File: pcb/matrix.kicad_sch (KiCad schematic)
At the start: 122 parts, among them SW1 SW_Push, SW10 SW_Push, SW11 SW_Push, SW12 SW_Push, SW13 SW_Push, SW14 SW_Push, SW15 SW_Push, SW16 SW_Push, SW17 SW_Push, SW18 SW_Push, SW19 SW_Push, SW2 SW_Push, SW20 SW_Push, SW21 SW_Push, SW22 SW_Push, SW23 SW_Push, SW24 SW_Push, SW25 SW_Push, SW26 SW_Push, SW27 SW_Push, SW28 SW_Push, SW29 SW_Push, SW3 SW_Push, SW30 SW_Push, SW31 SW_Push, SW32 SW_Push, SW33 SW_Push, SW34 SW_Push, SW35 SW_Push, SW36 SW_Push, SW37 SW_Push, SW38 SW_Push, SW39 SW_Push, SW4 SW_Push, SW40 SW_Push, SW41 SW_Push, SW42 SW_Push, SW43 SW_Push, SW44 SW_Push, SW45 SW_Push, SW46 SW_Push, SW47 SW_Push, SW48 SW_Push, SW49 SW_Push, SW5 SW_Push, SW50 SW_Push, SW51 SW_Push, SW52 SW_Push, SW53 SW_Push, SW54 SW_Push, SW55 SW_Push, SW56 SW_Push, SW57 SW_Push, SW58 SW_Push, SW59 SW_Push, SW6 SW_Push, SW60 SW_Push, SW61 SW_Push, SW7 SW_Push, SW8 SW_Push, SW9 SW_Push

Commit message: Fixed critical mistake where CAPSLOCK and Tab were indistinguishable
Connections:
- net COL0: no longer SW54.1
- net COL1: now also SW54.1; no longer SW55.1
- net COL2: now also SW55.1; no longer SW56.1
- net COL3: now also SW56.1; no longer SW57.1
- net COL4: now also SW57.1
- net ROW2: no longer D15.2 (A)
- net ROW4: now also D15.2 (A)
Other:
- note added: "TAB Moved to ROW4"
- note removed: "TAB is ROW2"
- moved on the sheet: D1, D15, D29, D42, D54, D55, D56, D57, SW1, SW15, SW29, SW42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

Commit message: Changed schematic header
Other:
- company: (none) -> agrantushinsky/simplekeyboard
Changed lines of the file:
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@@
 	(title_block
 		(title "Keyboard Matrix")
-		(date "2026-05-05")
+		(date "2026-07-18")
 		(rev "A")
+		(company "agrantushinsky/simplekeyboard")
 	)
 	(text "TAB Moved to ROW4"

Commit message: Changed spacebar to use reversed stabilizers
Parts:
- SW57: footprint ai03_MX:MX-Solderable-6.25U -> ai03_MX:MX-Solderable-6.25U-ReversedStabilizers
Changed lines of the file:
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@@
 			)
 		)
-		(property "Footprint" "ai03_MX:MX-Solderable-6.25U"
+		(property "Footprint" "ai03_MX:MX-Solderable-6.25U-ReversedStabilizers"
 			(at 115.57 121.92 0)
 			(effects

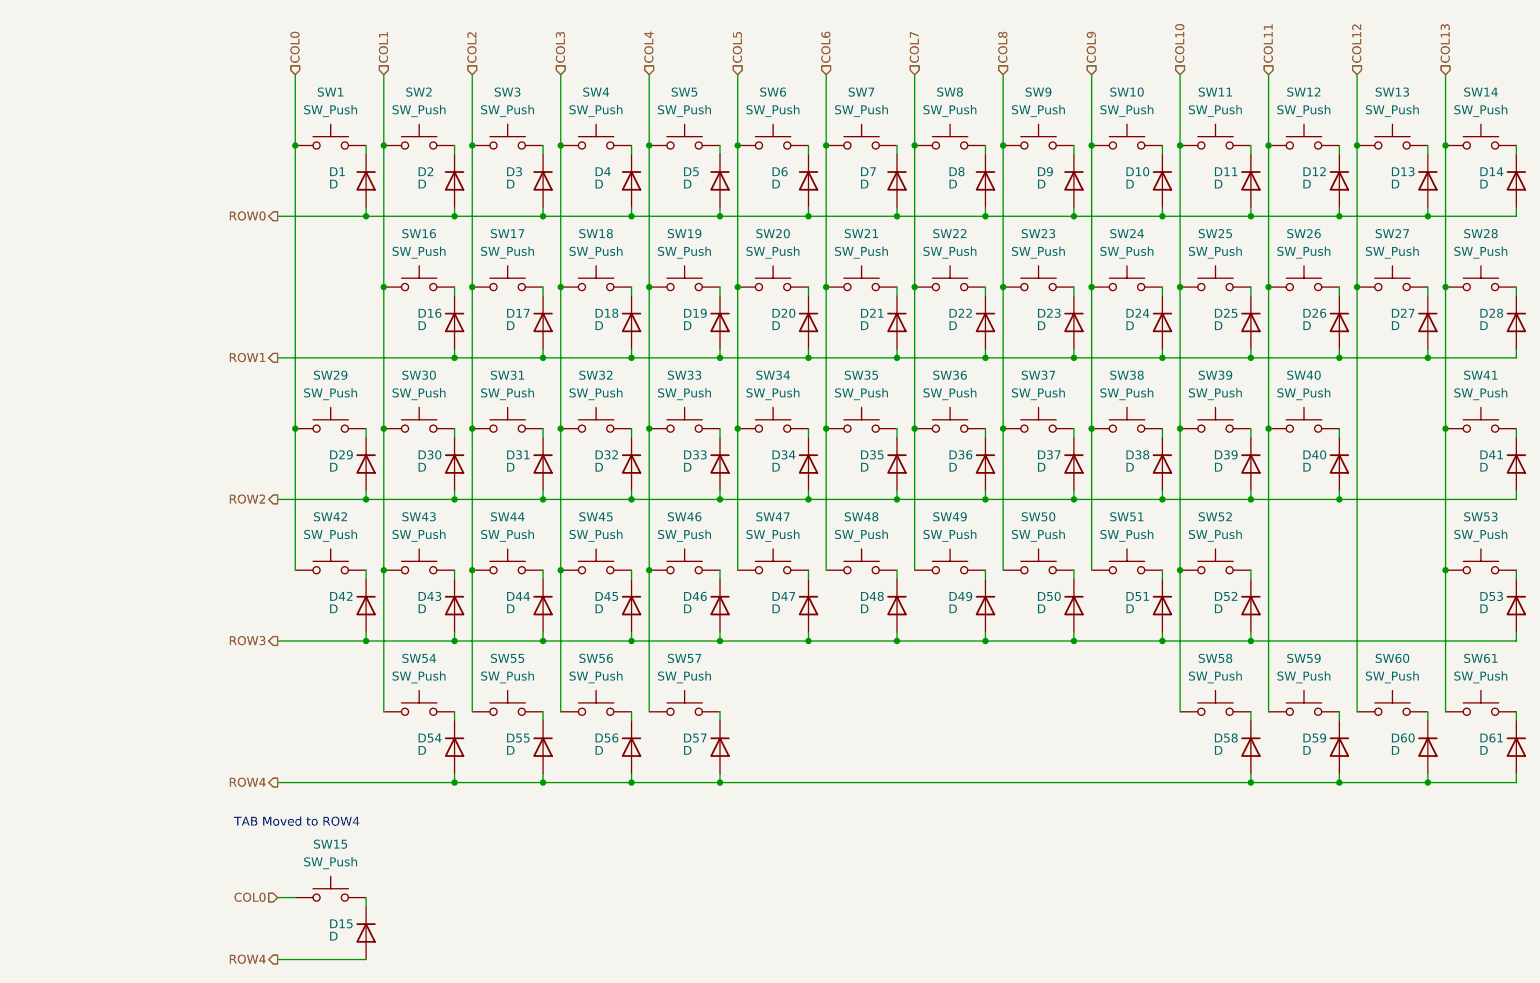
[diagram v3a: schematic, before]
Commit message: Fixed diode orientation and SDA/SCL
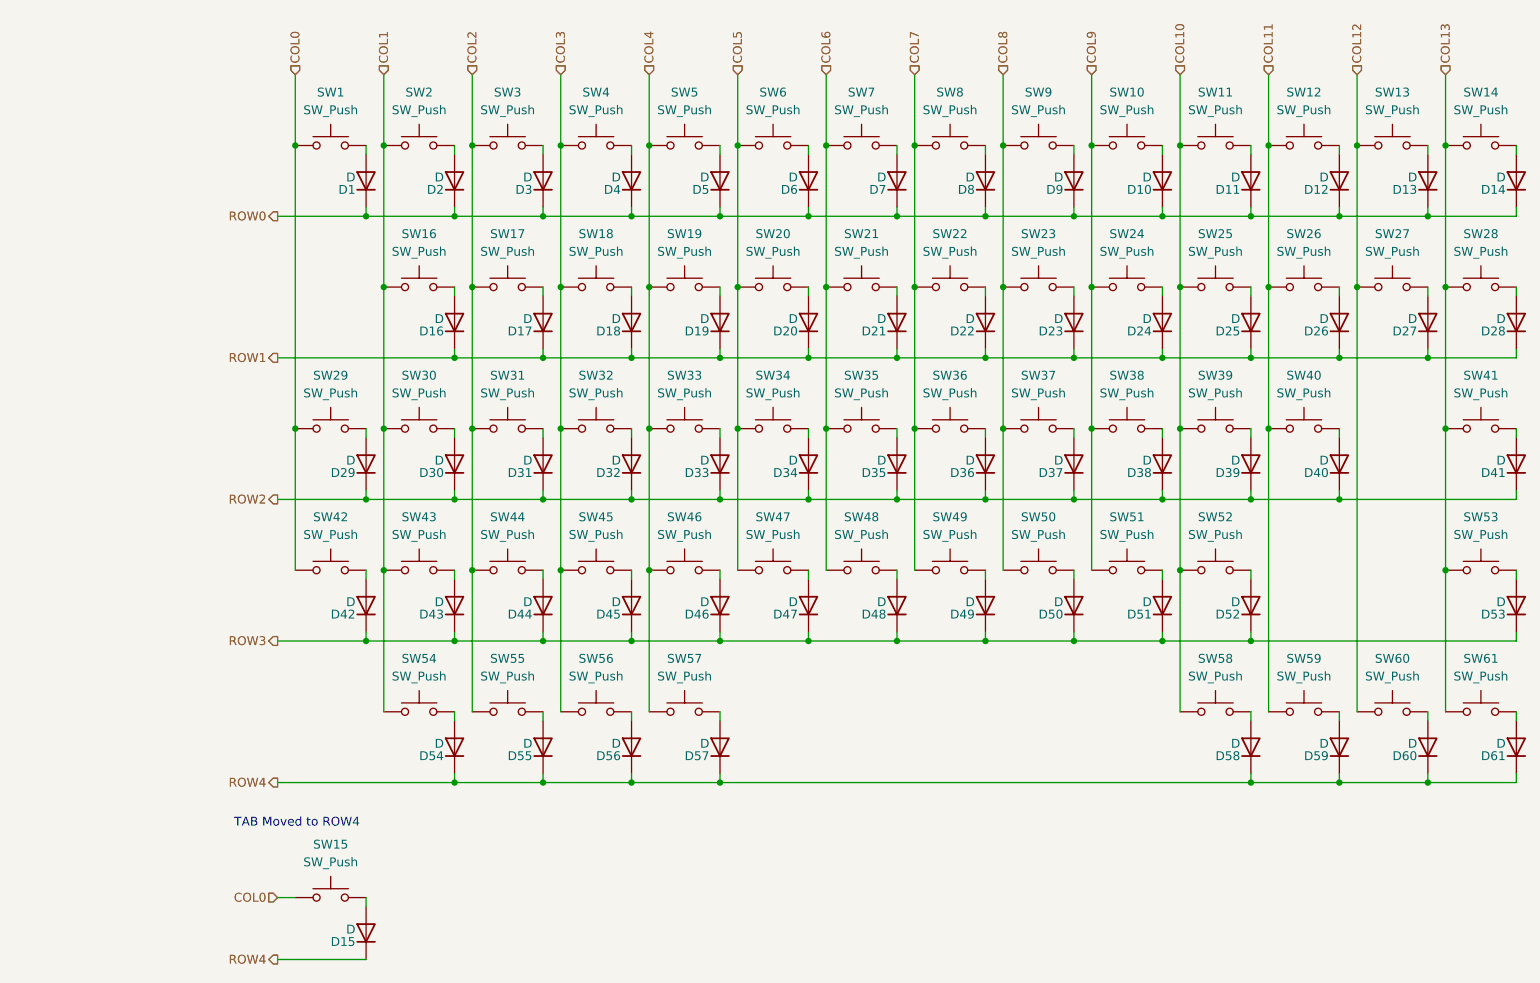
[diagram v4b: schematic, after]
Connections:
- net ROW0: now also D1.1 (K), D10.1 (K), D11.1 (K), D12.1 (K), D13.1 (K), D14.1 (K), D2.1 (K), D3.1 (K), D4.1 (K), D5.1 (K), D6.1 (K), D7.1 (K), D8.1 (K), D9.1 (K); no longer D1.2 (A), D10.2 (A), D11.2 (A), D12.2 (A), D13.2 (A), D14.2 (A), D2.2 (A), D3.2 (A), D4.2 (A), D5.2 (A), D6.2 (A), D7.2 (A), D8.2 (A), D9.2 (A)
- net ROW1: now also D16.1 (K), D17.1 (K), D18.1 (K), D19.1 (K), D20.1 (K), D21.1 (K), D22.1 (K), D23.1 (K), D24.1 (K), D25.1 (K), D26.1 (K), D27.1 (K), D28.1 (K); no longer D16.2 (A), D17.2 (A), D18.2 (A), D19.2 (A), D20.2 (A), D21.2 (A), D22.2 (A), D23.2 (A), D24.2 (A), D25.2 (A), D26.2 (A), D27.2 (A), D28.2 (A)
- net ROW2: now also D29.1 (K), D30.1 (K), D31.1 (K), D32.1 (K), D33.1 (K), D34.1 (K), D35.1 (K), D36.1 (K), D37.1 (K), D38.1 (K), D39.1 (K), D40.1 (K), D41.1 (K); no longer D29.2 (A), D30.2 (A), D31.2 (A), D32.2 (A), D33.2 (A), D34.2 (A), D35.2 (A), D36.2 (A), D37.2 (A), D38.2 (A), D39.2 (A), D40.2 (A), D41.2 (A)
- net ROW3: now also D42.1 (K), D43.1 (K), D44.1 (K), D45.1 (K), D46.1 (K), D47.1 (K), D48.1 (K), D49.1 (K), D50.1 (K), D51.1 (K), D52.1 (K), D53.1 (K); no longer D42.2 (A), D43.2 (A), D44.2 (A), D45.2 (A), D46.2 (A), D47.2 (A), D48.2 (A), D49.2 (A), D50.2 (A), D51.2 (A), D52.2 (A), D53.2 (A)
- net ROW4: now also D15.1 (K), D54.1 (K), D55.1 (K), D56.1 (K), D57.1 (K), D58.1 (K), D59.1 (K), D60.1 (K), D61.1 (K); no longer D15.2 (A), D54.2 (A), D55.2 (A), D56.2 (A), D57.2 (A), D58.2 (A), D59.2 (A), D60.2 (A), D61.2 (A)
- net at SW36.2: now also D36.2 (A); no longer D36.1 (K)
- net at SW28.2: now also D28.2 (A); no longer D28.1 (K)
- net at SW27.2: now also D27.2 (A); no longer D27.1 (K)
- net at SW43.2: now also D43.2 (A); no longer D43.1 (K)
- net at SW23.2: now also D23.2 (A); no longer D23.1 (K)
- net at SW15.2: now also D15.2 (A); no longer D15.1 (K)
- net at SW20.2: now also D20.2 (A); no longer D20.1 (K)
- net at SW33.2: now also D33.2 (A); no longer D33.1 (K)
- net at SW49.2: now also D49.2 (A); no longer D49.1 (K)
- net at SW53.2: now also D53.2 (A); no longer D53.1 (K)
- net at SW55.2: now also D55.2 (A); no longer D55.1 (K)
- net at SW19.2: now also D19.2 (A); no longer D19.1 (K)
- net at SW29.2: now also D29.2 (A); no longer D29.1 (K)
- net at SW14.2: now also D14.2 (A); no longer D14.1 (K)
- net at SW13.2: now also D13.2 (A); no longer D13.1 (K)
- net at SW60.2: now also D60.2 (A); no longer D60.1 (K)
- net at SW46.2: now also D46.2 (A); no longer D46.1 (K)
- net at SW32.2: now also D32.2 (A); no longer D32.1 (K)
- net at SW18.2: now also D18.2 (A); no longer D18.1 (K)
- net at SW34.2: now also D34.2 (A); no longer D34.1 (K)
- net at SW26.2: now also D26.2 (A); no longer D26.1 (K)
- net at SW54.2: now also D54.2 (A); no longer D54.1 (K)
- net at SW48.2: now also D48.2 (A); no longer D48.1 (K)
- net at SW24.2: now also D24.2 (A); no longer D24.1 (K)
- net at SW11.2: now also D11.2 (A); no longer D11.1 (K)
- net at SW17.2: now also D17.2 (A); no longer D17.1 (K)
- net at SW10.2: now also D10.2 (A); no longer D10.1 (K)
- net at SW58.2: now also D58.2 (A); no longer D58.1 (K)
- net at SW21.2: now also D21.2 (A); no longer D21.1 (K)
- net at SW39.2: now also D39.2 (A); no longer D39.1 (K)
- net at SW1.2: now also D1.2 (A); no longer D1.1 (K)
- net at SW9.2: now also D9.2 (A); no longer D9.1 (K)
- net at SW56.2: now also D56.2 (A); no longer D56.1 (K)
- net at SW59.2: now also D59.2 (A); no longer D59.1 (K)
- net at SW4.2: now also D4.2 (A); no longer D4.1 (K)
- net at SW41.2: now also D41.2 (A); no longer D41.1 (K)
- net at SW7.2: now also D7.2 (A); no longer D7.1 (K)
- net at SW22.2: now also D22.2 (A); no longer D22.1 (K)
- net at SW47.2: now also D47.2 (A); no longer D47.1 (K)
- net at SW6.2: now also D6.2 (A); no longer D6.1 (K)
- net at SW44.2: now also D44.2 (A); no longer D44.1 (K)
- net at SW37.2: now also D37.2 (A); no longer D37.1 (K)
- net at SW40.2: now also D40.2 (A); no longer D40.1 (K)
- net at SW50.2: now also D50.2 (A); no longer D50.1 (K)
- net at SW45.2: now also D45.2 (A); no longer D45.1 (K)
- net at SW42.2: now also D42.2 (A); no longer D42.1 (K)
- net at SW51.2: now also D51.2 (A); no longer D51.1 (K)
- net at SW2.2: now also D2.2 (A); no longer D2.1 (K)
- net at SW31.2: now also D31.2 (A); no longer D31.1 (K)
- net at SW52.2: now also D52.2 (A); no longer D52.1 (K)
- net at SW5.2: now also D5.2 (A); no longer D5.1 (K)
- net at SW30.2: now also D30.2 (A); no longer D30.1 (K)
- net at SW12.2: now also D12.2 (A); no longer D12.1 (K)
- net at SW16.2: now also D16.2 (A); no longer D16.1 (K)
- net at SW38.2: now also D38.2 (A); no longer D38.1 (K)
- net at SW8.2: now also D8.2 (A); no longer D8.1 (K)
- net at SW61.2: now also D61.2 (A); no longer D61.1 (K)
- net at SW3.2: now also D3.2 (A); no longer D3.1 (K)
- net at SW57.2: now also D57.2 (A); no longer D57.1 (K)
- net at SW35.2: now also D35.2 (A); no longer D35.1 (K)
- net at SW25.2: now also D25.2 (A); no longer D25.1 (K)
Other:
- moved on the sheet: D1
